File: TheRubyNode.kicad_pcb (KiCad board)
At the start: 2 copper layers, 141 x 79.5 mm, 66 parts, among them J1 USB4085-GF-A_REVB, J2 Conn_02x01, J3 Conn_02x01, J4 Conn_01x02, J5 91930-21111LF, J6 Conn_01x04, J7 Conn_01x03, J8 Conn_02x01, Q1 Si2307, SW1 SW_SPST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

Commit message: Finalise rev 1.0 of PCB
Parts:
- J6: footprint Connector_JST:JST_SH_SM04B-SRSS-TB_1x04-1MP_P1.00mm_Horizontal -> Connector_JST:JST_SH_BM04B-SRSS-TB_1x04-1MP_P1.00mm_Vertical
- moved J6 0.20 mm to (133.6, 100.8)
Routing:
- net I2C_SDA: track 94.4 -> 97.7 mm
- net I2C_SCL: track 90.8 -> 94.1 mm
- net +3V3: track 170.6 -> 173.7 mm
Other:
- board text added: "+5V IN"
- board text added: "+5V OUT"
- board text added: "REV v1.0"
- board text added: "USR BTN"

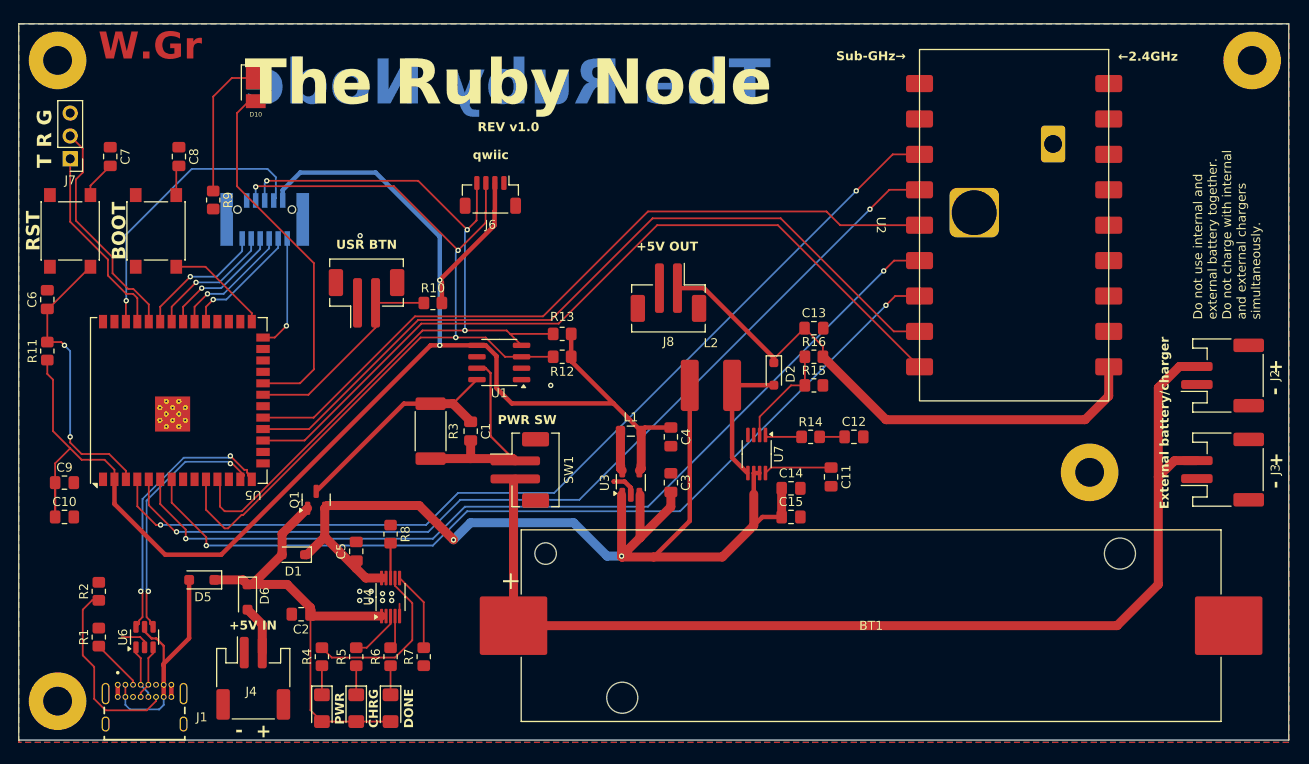
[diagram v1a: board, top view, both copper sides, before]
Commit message: Break out additional IOs
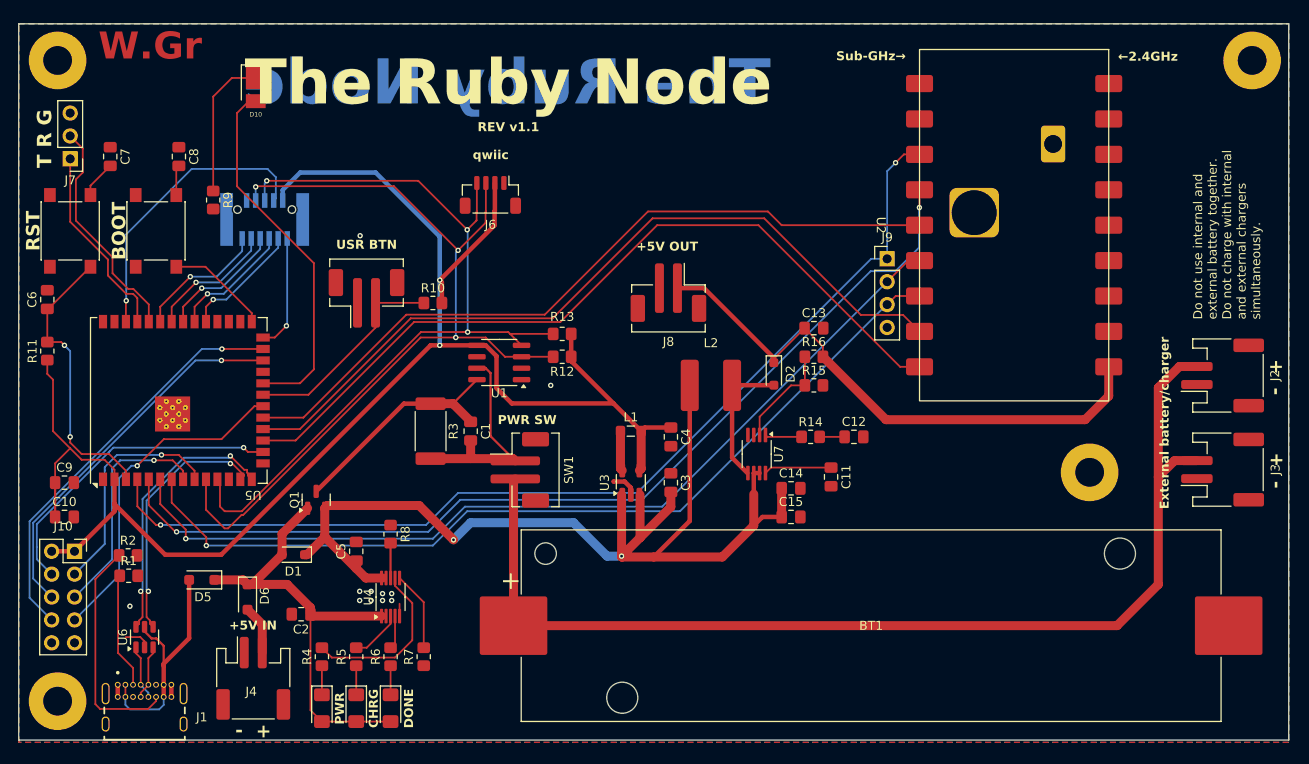
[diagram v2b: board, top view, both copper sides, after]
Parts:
- added J10: Conn_02x05_Odd_Even, Connector_PinSocket_2.54mm:PinSocket_2x05_P2.54mm_Vertical, F.Cu at (87.5, 140.3)
- added J9: Conn_01x04, Connector_PinHeader_2.54mm:PinHeader_1x04_P2.54mm_Vertical, F.Cu at (177.7, 107.9)
- moved R1 7.57 mm to (93.5, 143.1), turned to 0 degrees
- moved R2 5.15 mm to (93.4, 140.8), turned to 0 degrees
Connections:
- U5 pad 16: unconnected-(U5-IO46-Pad16) -> Net-(J10-Pin_4)
- U5 pad 20: unconnected-(U5-IO12-Pad20) -> Net-(J10-Pin_7)
- U5 pad 24: unconnected-(U5-IO47-Pad24) -> Net-(J10-Pin_6)
- U5 pad 25: unconnected-(U5-IO48-Pad25) -> Net-(J10-Pin_8)
- U5 pad 8: unconnected-(U5-IO15-Pad8) -> Net-(J10-Pin_5)
- U5 pad 9: unconnected-(U5-IO16-Pad9) -> Net-(J10-Pin_3)
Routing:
- net Net-(J10-Pin_8): track 0.00 -> 45.8 mm, vias 0 -> 1
- net Net-(J10-Pin_6): track 0.00 -> 42.1 mm, vias 0 -> 1
- net Net-(J10-Pin_7): track 0.00 -> 37.1 mm, vias 0 -> 1
- net Net-(J10-Pin_4): track 0.00 -> 35.1 mm, vias 0 -> 1
- net Net-(J10-Pin_5): track 0.00 -> 25.7 mm, vias 0 -> 1
- net Net-(J10-Pin_3): track 0.00 -> 25.5 mm, vias 0 -> 1
- net +3V3: track 173.7 -> 183.4 mm
- net Net-(J1-CC1): track 5.50 -> 12.9 mm
- net SPI_SCK: track 107.7 -> 113.4 mm
- net Net-(J1-CC2): track 20.9 -> 25.4 mm
- net LR_CS: track 105.5 -> 109.2 mm
- net GND: track 10.4 -> 9.98 mm, vias 10 -> 11
- net SPI_MISO: track 99.6 -> 99.4 mm, vias 2 -> 1
- net SPI_MOSI: vias 2 -> 1
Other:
- board text added: "REV v1.1"
- board text removed: "REV v1.0"

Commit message: Add pin labels
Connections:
- net Net-(J10-Pin_3) renamed /IO16
- net Net-(J10-Pin_4) renamed /IO46
- net Net-(J10-Pin_5) renamed /IO15
- net Net-(J10-Pin_6) renamed /IO47
- net Net-(J10-Pin_7) renamed /IO12
- net Net-(J10-Pin_8) renamed /IO48
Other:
- board text added: "12"
- board text added: "15"
- board text added: "16"
- board text added: "3V3"
- board text added: "46"
- board text added: "47"
- board text added: "48"
- board text added: "GND"
- board text added: "REV v1.2"
- board text removed: "REV v1.1"
